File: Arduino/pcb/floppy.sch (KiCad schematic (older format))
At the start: 11 parts, among them J7 Floppy-Power, J8 IBM_PC_Floppy_IDC, SW1 Bus Address Select, U1 4021

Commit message: pcb: did... something
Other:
- moved on the sheet: C2, J7, J8
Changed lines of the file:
@@
 Comment4 ""
 $EndDescr
-NoConn ~ 6075 2925
-NoConn ~ 6075 3025
-NoConn ~ 6075 3325
-NoConn ~ 6075 3625
-NoConn ~ 6075 3725
-NoConn ~ 6075 3925
-NoConn ~ 6075 4025
-NoConn ~ 6075 4125
-NoConn ~ 6075 4225
-NoConn ~ 6075 2625
-NoConn ~ 6075 3225
+NoConn ~ 6950 2925
+NoConn ~ 6950 3025
+NoConn ~ 6950 3325
+NoConn ~ 6950 3625
+NoConn ~ 6950 3725
+NoConn ~ 6950 3925
+NoConn ~ 6950 4025
+NoConn ~ 6950 4125
+NoConn ~ 6950 4225
+NoConn ~ 6950 2625
+NoConn ~ 6950 3225
 $Comp
 L ibm_pc_floppy_idc:IBM_PC_Floppy_IDC J?
 U 1 1 5CE26438
-P 6875 3425
+P 7750 3425
 AR Path="/5CE26438" Ref="J?"  Part="1"
 AR Path="/5CD0EE48/5CE26438" Ref="J8"  Part="1"
-F 0 "J8" H 7075 4475 50  0000 C CNN
-F 1 "IBM_PC_Floppy_IDC" H 7125 4375 50  0000 C CNN
-F 2 "ibm_idc_floppy_connector:ibm_pc_floppy_idc" H 6875 3425 50  0001 C CNN
-F 3 "" H 6875 3425 50  0001 C CNN
-	1    6875 3425
+F 0 "J8" H 7950 4475 50  0000 C CNN
+F 1 "IBM_PC_Floppy_IDC" H 8000 4375 50  0000 C CNN
+F 2 "ibm_idc_floppy_connector:ibm_pc_floppy_idc" H 7750 3425 50  0001 C CNN
+F 3 "" H 7750 3425 50  0001 C CNN
+	1    7750 3425
 	-1   0    0    -1
 $EndComp
 Wire Wire Line
-	7075 2625 7075 2725
-Connection ~ 7075 2725
-Wire Wire Line
-	7075 2725 7075 2825
-Connection ~ 7075 2825
-Wire Wire Line
-	7075 2825 7075 2925
-Connection ~ 7075 2925
-Wire Wire Line
-	7075 2925 7075 3025
-Connection ~ 7075 3025
-Wire Wire Line
-	7075 3025 7075 3125
-Connection ~ 7075 3125
-Wire Wire Line
-	7075 3125 7075 3225
-Connection ~ 7075 3225
-Wire Wire Line
-	7075 3225 7075 3325
-Connection ~ 7075 3325
-Wire Wire Line
-	7075 3325 7075 3425
-Connection ~ 7075 3425
-Wire Wire Line
-	7075 3425 7075 3525
-Connection ~ 7075 3525
-Wire Wire Line
-	7075 3525 7075 3625
-Connection ~ 7075 3625
-Wire Wire Line
-	7075 3625 7075 3725
-Connection ~ 7075 3725
-Wire Wire Line
-	7075 3725 7075 3825
-Connection ~ 7075 3825
-Wire Wire Line
-	7075 3825 7075 3925
-Connection ~ 7075 3925
-Wire Wire Line
-	7075 3925 7075 4025
-Connection ~ 7075 4025
-Wire Wire Line
-	7075 4025 7075 4125
-Wire Wire Line
-	7075 4125 7075 4225
-Connection ~ 7075 4125
-Connection ~ 7075 4225
-Wire Wire Line
-	7075 4225 7075 4425
+	7950 2625 7950 2725
+Connection ~ 7950 2725
+Wire Wire Line
+	7950 2725 7950 2825
+Connection ~ 7950 2825
+Wire Wire Line
+	7950 2825 7950 2925
+Connection ~ 7950 2925
+Wire Wire Line
+	7950 2925 7950 3025
+Connection ~ 7950 3025
+Wire Wire Line
+	7950 3025 7950 3125
+Connection ~ 7950 3125
+Wire Wire Line
+	7950 3125 7950 3225
+Connection ~ 7950 3225
+Wire Wire Line
+	7950 3225 7950 3325
+Connection ~ 7950 3325
+Wire Wire Line
+	7950 3325 7950 3425
+Connection ~ 7950 3425
+Wire Wire Line
+	7950 3425 7950 3525
+Connection ~ 7950 3525
+Wire Wire Line
+	7950 3525 7950 3625
+Connection ~ 7950 3625
+Wire Wire Line
+	7950 3625 7950 3725
+Connection ~ 7950 3725
+Wire Wire Line
+	7950 3725 7950 3825
+Connection ~ 7950 3825
+Wire Wire Line
+	7950 3825 7950 3925
+Connection ~ 7950 3925
+Wire Wire Line
+	7950 3925 7950 4025
+Connection ~ 7950 4025
+Wire Wire Line
+	7950 4025 7950 4125
+Wire Wire Line
+	7950 4125 7950 4225
+Connection ~ 7950 4125
+Connection ~ 7950 4225
+Wire Wire Line
+	7950 4225 7950 4425
 $Comp
 L power:GND #PWR?
 U 1 1 5CE2645F
-P 7075 4425
+P 7950 4425
 AR Path="/5CE2645F" Ref="#PWR?"  Part="1"
 AR Path="/5CD0EE48/5CE2645F" Ref="#PWR018"  Part="1"
-F 0 "#PWR018" H 7075 4175 50  0001 C CNN
-F 1 "GND" H 7080 4252 50  0000 C CNN
-F 2 "" H 7075 4425 50  0001 C CNN
-F 3 "" H 7075 4425 50  0001 C CNN
-	1    7075 4425
+F 0 "#PWR018" H 7950 4175 50  0001 C CNN
+F 1 "GND" H 7955 4252 50  0000 C CNN
+F 2 "" H 7950 4425 50  0001 C CNN
+F 3 "" H 7950 4425 50  0001 C CNN
+	1    7950 4425
 	-1   0    0    -1
 $EndComp
-Text HLabel 5975 3125 0    50   Input ~ 0
+Text HLabel 6850 3125 0    50   Input ~ 0
 DRIVE_SELECT
-Text HLabel 5975 3425 0    50   Input ~ 0
+Text HLabel 6850 3425 0    50   Input ~ 0
 DIRECTION
-Text HLabel 5975 3825 0    50   Output ~ 0
+Text HLabel 6850 3825 0    50   Output ~ 0
 TRK00
-Text HLabel 5975 3525 0    50   Input ~ 0
+Text HLabel 6850 3525 0    50   Input ~ 0
 STEP
 Wire Wire Line
-	5975 3125 6075 3125
-Wire Wire Line
-	5975 3425 6075 3425
-Wire Wire Line
-	5975 3525 6075 3525
-Wire Wire Line
-	5975 3825 6075 3825
+	6850 3125 6950 3125
+Wire Wire Line
+	6850 3425 6950 3425
+Wire Wire Line
+	6850 3525 6950 3525
+Wire Wire Line
+	6850 3825 6950 3825
 $Comp
 L floppy-power:Floppy-Power J?
 U 1 1 5CEBDDC6
-P 1975 1925
+P 7625 1675
 AR Path="/5CEBDDC6" Ref="J?"  Part="1"
 AR Path="/5CD0EE48/5CEBDDC6" Ref="J7"  Part="1"
-F 0 "J7" H 2025 2275 50  0000 L CNN
-F 1 "Floppy-Power" H 1825 2175 50  0000 L CNN
-F 2 "floppy_power:Floppy_Power_1x04_Pitch2.54mm" H 1975 1925 50  0001 C CNN
-F 3 "" H 1975 1925 50  0001 C CNN
-	1    1975 1925
+F 0 "J7" H 7675 2025 50  0000 L CNN
+F 1 "Floppy-Power" H 7475 1925 50  0000 L CNN
+F 2 "floppy_power:Floppy_Power_1x04_Pitch2.54mm" H 7625 1675 50  0001 C CNN
+F 3 "" H 7625 1675 50  0001 C CNN
+	1    7625 1675
 	1    0    0    -1
 $EndComp
@@
 L power:GND #PWR?
 U 1 1 5CEBDDD4
-P 1600 1925
+P 7250 1675
 AR Path="/5CEBDDD4" Ref="#PWR?"  Part="1"
 AR Path="/5CD0EE48/5CEBDDD4" Ref="#PWR010"  Part="1"
-F 0 "#PWR010" H 1600 1675 50  0001 C CNN
-F 1 "GND" H 1605 1752 50  0000 C CNN
-F 2 "" H 1600 1925 50  0001 C CNN
-F 3 "" H 1600 1925 50  0001 C CNN
-	1    1600 1925
-	1    0    0    -1
-$EndComp
-Wire Wire Line
-	1775 2025 1775 1925
-Connection ~ 1775 1925
-Wire Wire Line
-	1600 1925 1775 1925
-Wire Wire Line
-	1775 2275 1775 2125
-Wire Wire Line
-	1600 1825 1775 1825
-Text HLabel 1600 1825 0    50   Input ~ 0
+F 0 "#PWR010" H 7250 1425 50  0001 C CNN
+F 1 "GND" H 7255 1502 50  0000 C CNN
+F 2 "" H 7250 1675 50  0001 C CNN
+F 3 "" H 7250 1675 50  0001 C CNN
+	1    7250 1675
+	1    0    0    -1
+$EndComp
+Wire Wire Line
+	7425 1775 7425 1675
+Connection ~ 7425 1675
+Wire Wire Line
+	7250 1675 7425 1675
+Wire Wire Line
+	7425 2025 7425 1875
+Wire Wire Line
+	7250 1575 7425 1575
+Text HLabel 7250 1575 0    50   Input ~ 0
 5V_BUS
-Text HLabel 1600 2275 0    50   Input ~ 0
+Text HLabel 7250 2025 0    50   Input ~ 0
 12V_BUS
 Wire Wire Line
-	1600 2275 1775 2275
+	7250 2025 7425 2025
 $Comp
 L floppyorgel-rescue:SW_DIP_x06-switches SW?
@@
 L Device:C C?
 U 1 1 5CD16AEF
-P 3300 1725
+P 5600 3200
 AR Path="/5CD16AEF" Ref="C?"  Part="1"
 AR Path="/5CCFEC3E/5CD16AEF" Ref="C?"  Part="1"
 AR Path="/5CD1E0A5/5CD16AEF" Ref="C?"  Part="1"
 AR Path="/5CD0EE48/5CD16AEF" Ref="C2"  Part="1"
-F 0 "C2" H 3075 1925 50  0000 L CNN
-F 1 "100nF" H 3025 1825 50  0000 L CNN
-F 2 "Capacitor_SMD:C_0805_2012Metric" H 3338 1575 50  0001 C CNN
-F 3 "~" H 3300 1725 50  0001 C CNN
-	1    3300 1725
+F 0 "C2" H 5375 3400 50  0000 L CNN
+F 1 "100nF" H 5325 3300 50  0000 L CNN
+F 2 "Capacitor_SMD:C_0805_2012Metric" H 5638 3050 50  0001 C CNN
+F 3 "~" H 5600 3200 50  0001 C CNN
+	1    5600 3200
 	1    0    0    -1
 $EndComp
@@
 L power:VCC #PWR?
 U 1 1 5CD16AF5
-P 3300 1450
+P 5600 2925
 AR Path="/5CCFEC3E/5CD16AF5" Ref="#PWR?"  Part="1"
 AR Path="/5CD1E0A5/5CD16AF5" Ref="#PWR?"  Part="1"
 AR Path="/5CD0EE48/5CD16AF5" Ref="#PWR014"  Part="1"
-F 0 "#PWR014" H 3300 1300 50  0001 C CNN
-F 1 "VCC" H 3317 1623 50  0000 C CNN
-F 2 "" H 3300 1450 50  0001 C CNN
-F 3 "" H 3300 1450 50  0001 C CNN
-	1    3300 1450
+F 0 "#PWR014" H 5600 2775 50  0001 C CNN
+F 1 "VCC" H 5617 3098 50  0000 C CNN
+F 2 "" H 5600 2925 50  0001 C CNN
+F 3 "" H 5600 2925 50  0001 C CNN
+	1    5600 2925
 	1    0    0    -1
 $EndComp
@@
 L power:GND #PWR?
 U 1 1 5CD16AFB
-P 3300 1975
+P 5600 3450
 AR Path="/5CCFEC3E/5CD16AFB" Ref="#PWR?"  Part="1"
 AR Path="/5CD1E0A5/5CD16AFB" Ref="#PWR?"  Part="1"
 AR Path="/5CD0EE48/5CD16AFB" Ref="#PWR015"  Part="1"
-F 0 "#PWR015" H 3300 1725 50  0001 C CNN
-F 1 "GND" H 3305 1802 50  0000 C CNN
-F 2 "" H 3300 1975 50  0001 C CNN
-F 3 "" H 3300 1975 50  0001 C CNN
-	1    3300 1975
-	1    0    0    -1
-$EndComp
-Wire Wire Line
-	3300 1450 3300 1575
-Wire Wire Line
-	3300 1875 3300 1975
-Text Notes 2925 1400 0    50   ~ 0
+F 0 "#PWR015" H 5600 3200 50  0001 C CNN
+F 1 "GND" H 5605 3277 50  0000 C CNN
+F 2 "" H 5600 3450 50  0001 C CNN
+F 3 "" H 5600 3450 50  0001 C CNN
+	1    5600 3450
+	1    0    0    -1
+$EndComp
+Wire Wire Line
+	5600 2925 5600 3050
+Wire Wire Line
+	5600 3350 5600 3450
+Text Notes 5225 2875 0    50   ~ 0
 Bypass
 $EndSCHEMATC

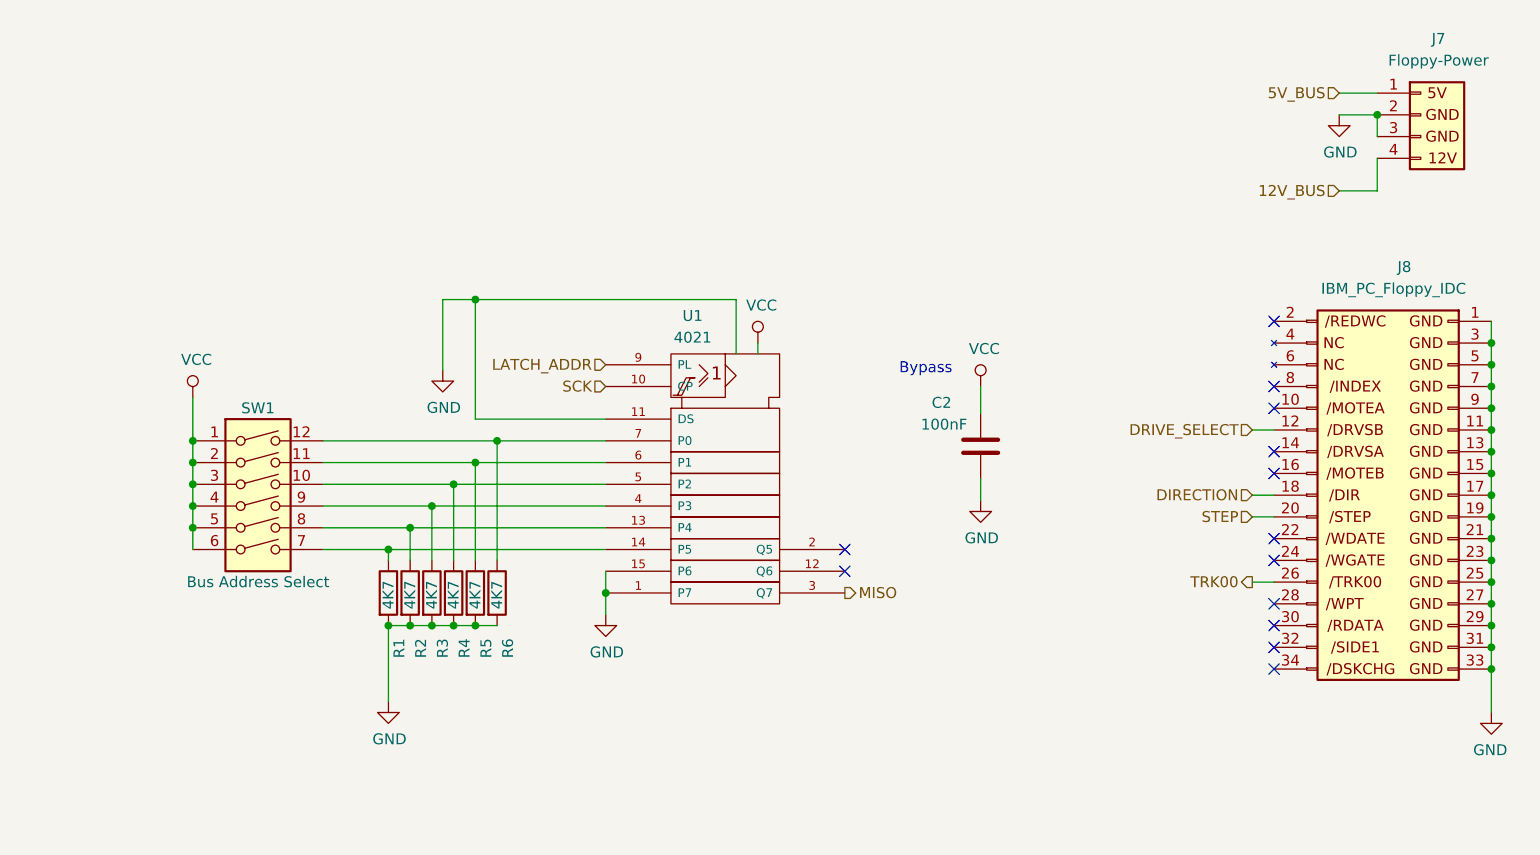
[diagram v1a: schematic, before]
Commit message: pcb / floppy: remove 4094 shift register / connect address connector directly
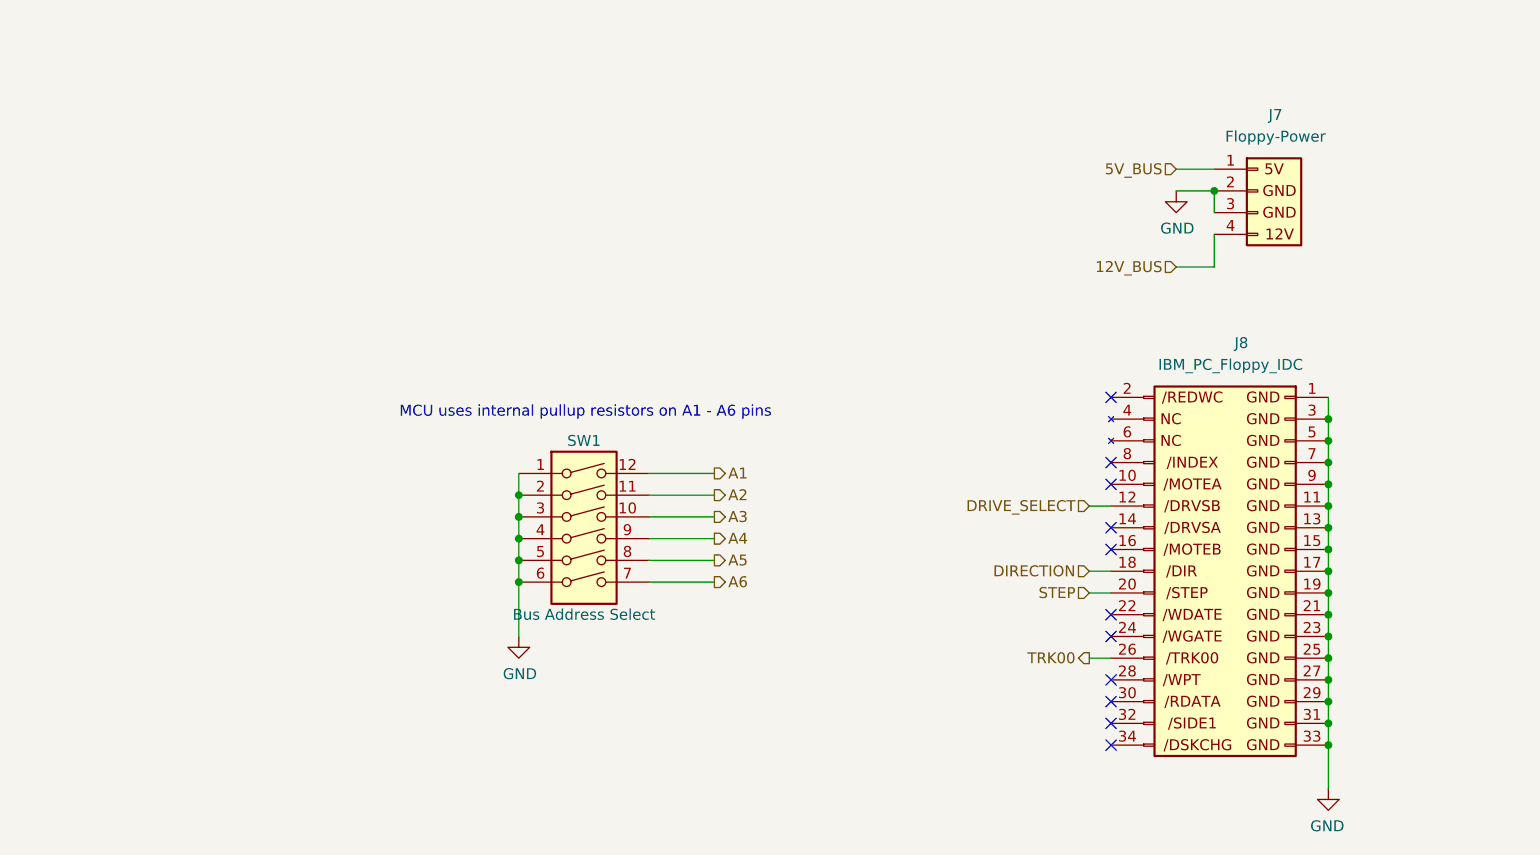
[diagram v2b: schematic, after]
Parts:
- removed C2: 100nF, Capacitor_SMD:C_0805_2012Metric, symbol Device:C
- removed R1, R2, R3, R4, R5, R6: 4K7, Resistor_SMD:R_0805_2012Metric, symbol Device:R
- removed U1: 4021, Package_SO:SSOP-16_5.3x6.2mm_P0.65mm, symbol 4xxx_IEEE:4021
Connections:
- net VCC is gone; now on net GND: SW1.1, SW1.2, SW1.3, SW1.4, SW1.5, SW1.6
- net A3: now reaches SW1.10
- net A2: now reaches SW1.11
- net A1: now reaches SW1.12
- net A6: now reaches SW1.7
- net A5: now reaches SW1.8
- net A4: now reaches SW1.9
- no-connect marks 13 -> 11
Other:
- note added: "MCU uses internal pullup resistors on A1 - A6 pins"
- note removed: "Bypass"
- moved on the sheet: J7, J8, SW1

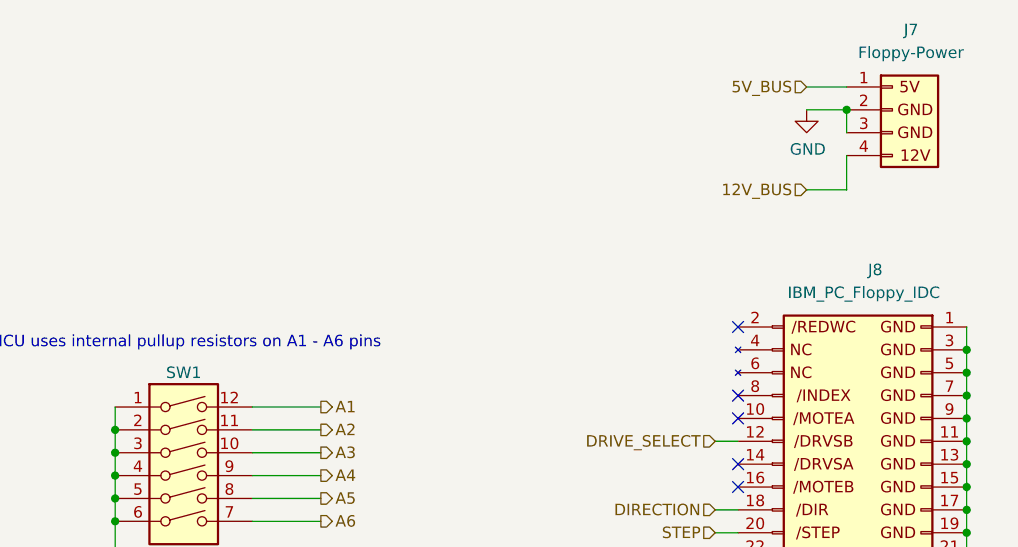
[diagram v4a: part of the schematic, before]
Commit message: pcb: reannotate symbols
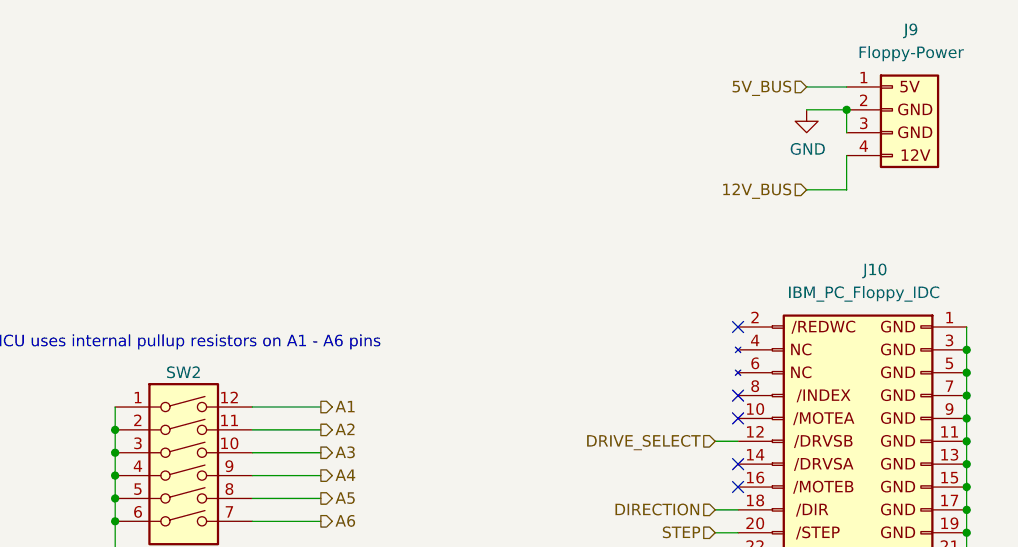
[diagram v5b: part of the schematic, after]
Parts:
- renumbered J8 to J10, J7 to J9, SW1 to SW2
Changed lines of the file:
@@
 P 7000 3775
 AR Path="/5CE26438" Ref="J?"  Part="1"
-AR Path="/5CD0EE48/5CE26438" Ref="J8"  Part="1"
-F 0 "J8" H 7200 4825 50  0000 C CNN
+AR Path="/5CD0EE48/5CE26438" Ref="J10"  Part="1"
+F 0 "J10" H 7200 4825 50  0000 C CNN
 F 1 "IBM_PC_Floppy_IDC" H 7250 4725 50  0000 C CNN
 F 2 "ibm_idc_floppy_connector:ibm_pc_floppy_idc" H 7000 3775 50  0001 C CNN
@@
 P 7200 4775
 AR Path="/5CE2645F" Ref="#PWR?"  Part="1"
-AR Path="/5CD0EE48/5CE2645F" Ref="#PWR018"  Part="1"
-F 0 "#PWR018" H 7200 4525 50  0001 C CNN
+AR Path="/5CD0EE48/5CE2645F" Ref="#PWR037"  Part="1"
+F 0 "#PWR037" H 7200 4525 50  0001 C CNN
 F 1 "GND" H 7205 4602 50  0000 C CNN
 F 2 "" H 7200 4775 50  0001 C CNN
@@
 P 6875 2025
 AR Path="/5CEBDDC6" Ref="J?"  Part="1"
-AR Path="/5CD0EE48/5CEBDDC6" Ref="J7"  Part="1"
-F 0 "J7" H 6925 2375 50  0000 L CNN
+AR Path="/5CD0EE48/5CEBDDC6" Ref="J9"  Part="1"
+F 0 "J9" H 6925 2375 50  0000 L CNN
 F 1 "Floppy-Power" H 6725 2275 50  0000 L CNN
 F 2 "floppy_power:Floppy_Power_1x04_Pitch2.54mm" H 6875 2025 50  0001 C CNN
@@
 P 6500 2025
 AR Path="/5CEBDDD4" Ref="#PWR?"  Part="1"
-AR Path="/5CD0EE48/5CEBDDD4" Ref="#PWR010"  Part="1"
-F 0 "#PWR010" H 6500 1775 50  0001 C CNN
+AR Path="/5CD0EE48/5CEBDDD4" Ref="#PWR036"  Part="1"
+F 0 "#PWR036" H 6500 1775 50  0001 C CNN
 F 1 "GND" H 6505 1852 50  0000 C CNN
 F 2 "" H 6500 2025 50  0001 C CNN
@@
 AR Path="/5D1F809D" Ref="SW?"  Part="1"
 AR Path="/5CD1E0A5/5D1F809D" Ref="SW?"  Part="1"
-AR Path="/5CD0EE48/5D1F809D" Ref="SW1"  Part="1"
-F 0 "SW1" H 3775 4075 50  0000 C CNN
+AR Path="/5CD0EE48/5D1F809D" Ref="SW2"  Part="1"
+F 0 "SW2" H 3775 4075 50  0000 C CNN
 F 1 "Bus Address Select" H 3775 3275 50  0000 C CNN
 F 2 "Button_Switch_THT:SW_DIP_SPSTx06_Slide_9.78x17.42mm_W7.62mm_P2.54mm" H 3775 3625 50  0001 C CNN
@@
 A6
 $Comp
-L power:GND #PWR0104
+L power:GND #PWR035
 U 1 1 5D9BC161
 P 3475 4075
-F 0 "#PWR0104" H 3475 3825 50  0001 C CNN
+F 0 "#PWR035" H 3475 3825 50  0001 C CNN
 F 1 "GND" H 3480 3902 50  0000 C CNN
 F 2 "" H 3475 4075 50  0001 C CNN
